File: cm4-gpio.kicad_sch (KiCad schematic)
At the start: 13 parts, among them SW1 SW_Push, SW2 SW_Push, U1 74LVC1G07SE-7, U2 74LVC1G07SE-7, U8 74154

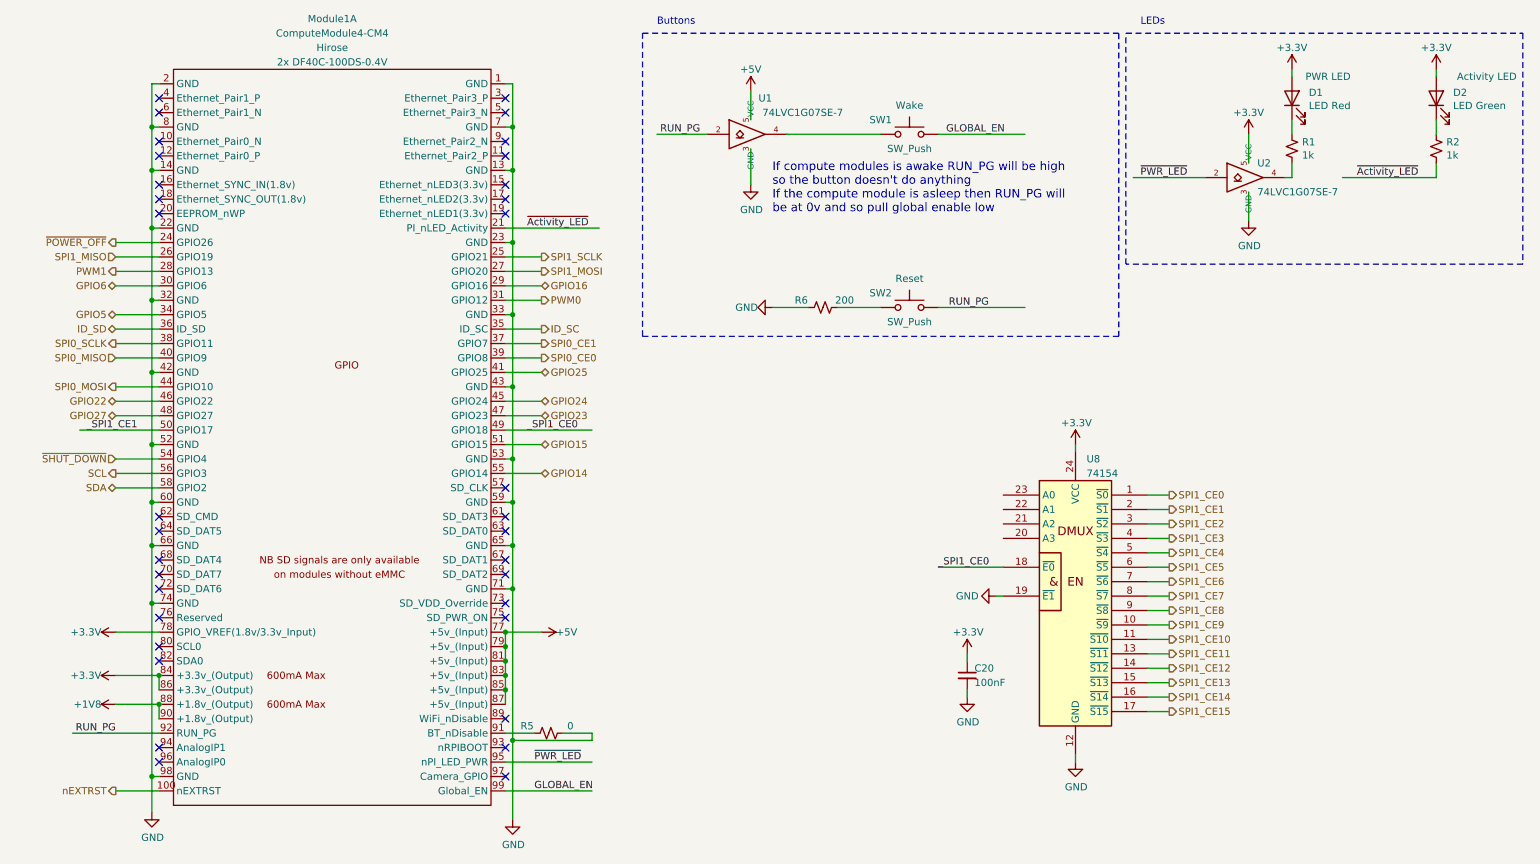
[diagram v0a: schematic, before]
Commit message: Allocate GPIOs.
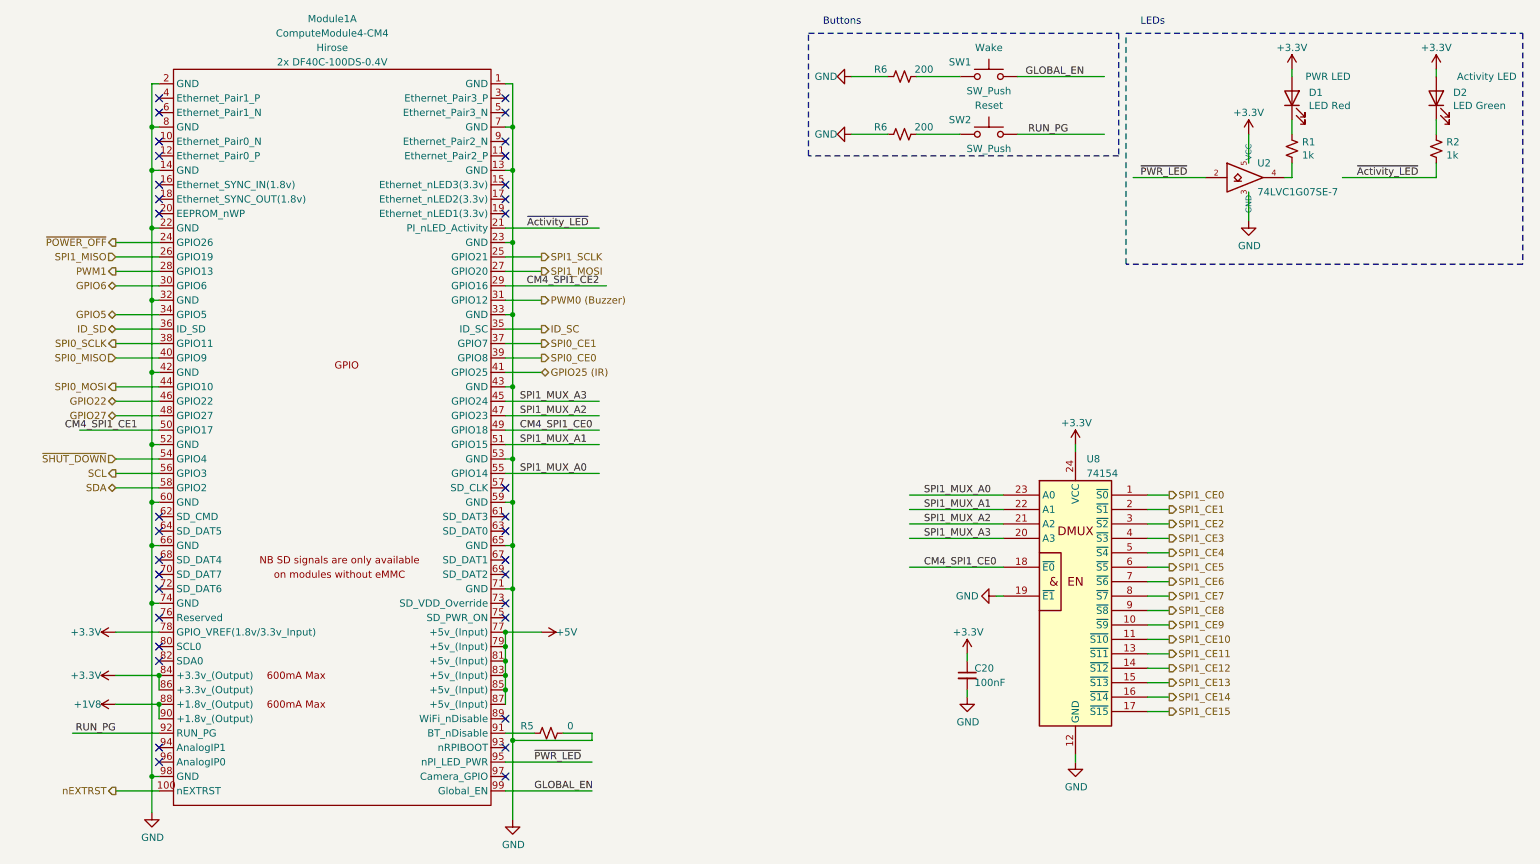
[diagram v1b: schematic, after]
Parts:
- removed U1: 74LVC1G07SE-7, Package_TO_SOT_SMD:SOT-353_SC-70-5, symbol 74lvc1g07:74LVC1G07
- added R6: 200, symbol Device:R_Small_US
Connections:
- net GPIO14 is gone; now on net SPI1_MUX_A0: Module1.55 (GPIO14)
- net GPIO15 is gone; now on net SPI1_MUX_A1: Module1.51 (GPIO15)
- net GPIO23 is gone; now on net SPI1_MUX_A2: Module1.47 (GPIO23)
- net GPIO24 is gone; now on net SPI1_MUX_A3: Module1.45 (GPIO24)
- net GND: now also R6.1
- net at SW1.1: now also R6.2
- net SPI1_MUX_A3: now reaches U8.20 (A3)
- net SPI1_MUX_A2: now reaches U8.21 (A2)
- net SPI1_MUX_A1: now reaches U8.22 (A1)
- net SPI1_MUX_A0: now reaches U8.23 (A0)
- net GPIO16 renamed CM4_SPI1_CE2
- net GPIO25 renamed GPIO25 (IR)
- net PWM0 renamed PWM0 (Buzzer)
- net _SPI1_CE0 renamed CM4_SPI1_CE0
- net _SPI1_CE1 renamed CM4_SPI1_CE1
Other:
- note removed: "If compute modules is awake RUN_PG will be high so the button doesn't do anything If the compute module is asleep then RUN_PG will be at 0v and so pull global enable low"
- moved on the sheet: R6, SW1, SW2
